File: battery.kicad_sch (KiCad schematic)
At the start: 41 parts, among them J15 Conn_01x02_Pin, J3 Lipo, Q2 AO3401A, Q3 IRLZ44N, Q4 IRLZ44N, Q5 2N7002, SW2 SW_Push, U2 BQ76920PW

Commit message: more lcsc part labels for non generic components
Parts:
- F1: LCSC (none) -> C3762600
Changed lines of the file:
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@@
 			)
 		)
-		(property "LCSC" ""
+		(property "LCSC" "C3762600"
 			(at 105.41 143.51 90)
 			(effects

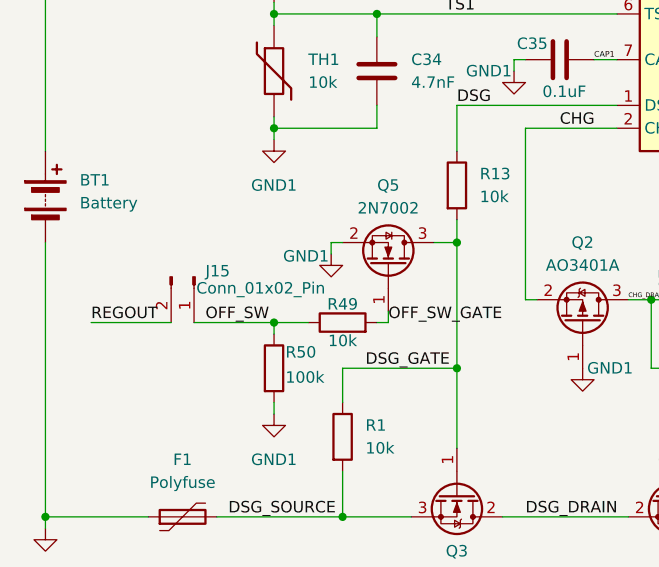
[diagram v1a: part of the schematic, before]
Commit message: Updated edge cuts and drawings from earlier fusion changes and moved traces accordingly
Also fixed jst connectors
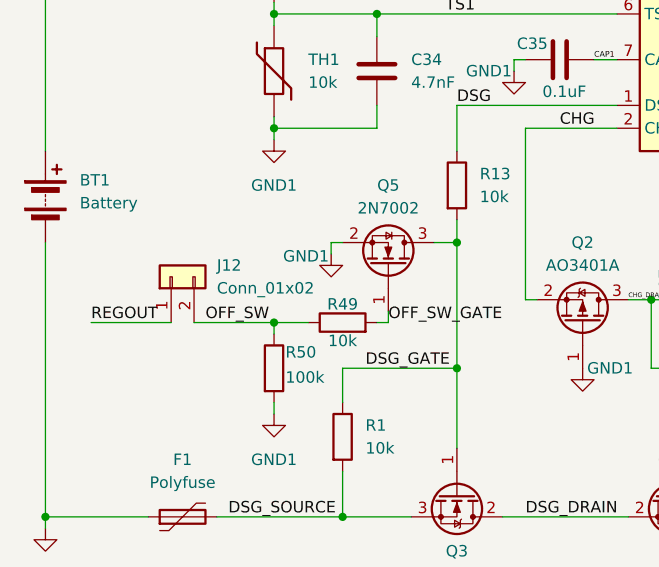
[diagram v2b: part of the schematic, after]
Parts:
- removed J15: Conn_01x02_Pin, Connector:JWT_A3963_1x02_P3.96mm_Vertical, symbol Connector:Conn_01x02_Pin
- added J12: Conn_01x02, Connector_JST:JST_PH_S2B-PH-K_1x02_P2.00mm_Horizontal, symbol Connector_Generic:Conn_01x02
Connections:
- net OFF_SW: now also J12.2 (Pin_2)
- net REGOUT: now also J12.1 (Pin_1)
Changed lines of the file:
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@@
+	)
+	(symbol
+		(lib_id "Connector_Generic:Conn_01x02")
+		(at 104.14 116.84 90)
+		(unit 1)
+		(exclude_from_sim no)
+		(in_bom yes)
+		(on_board yes)
+		(dnp no)
+		(fields_autoplaced yes)
+		(property "Reference" "J12"
+			(at 109.22 115.5699 90)
+			(effects
+				(font
+					(size 1.27 1.27)
+				)
+				(justify right)
+			)
+		)
+		(property "Value" "Conn_01x02"
+			(at 109.22 118.1099 90)
+			(effects
+				(font
+					(size 1.27 1.27)
+				)
+				(justify right)
+			)
+		)
+		(property "Footprint" "Connector_JST:JST_PH_S2B-PH-K_1x02_P2.00mm_Horizontal"
+			(at 104.14 116.84 0)
+			(effects
+				(font
+					(size 1.27 1.27)
+				)
+				(hide yes)
+			)
+		)
+		(property "Datasheet" "~"
+			(at 104.14 116.84 0)
+			(effects
+				(font
+					(size 1.27 1.27)
+				)
+				(hide yes)
+			)
+		)
+		(property "Description" "Generic connector, single row, 01x02, script generated (kicad-library-utils/schlib/autogen/connector/)"
+			(at 104.14 116.84 0)
+			(effects
+				(font
+					(size 1.27 1.27)
+				)
+				(hide yes)
+			)
+		)
+		(pin "1"
+		)
+		(pin "2"
+		)
+		(instances
+			(project ""
+				(path "/2f56b371-1597-47e1-a48d-b7f69d342f77/8e993949-53ac-4d46-9f7d-59c9cf3d33c4"
+					(reference "J12")
+					(unit 1)
+				)
+			)
+		)
 	)
 	(symbol
@@
 					(unit 1)
 				)
-			)
-		)
-	)
-	(symbol
-		(lib_id "Connector:Conn_01x02_Pin")
-		(at 106.68 116.84 270)
-		(unit 1)
-		(exclude_from_sim no)
-		(in_bom yes)
-		(on_board yes)
-		(dnp no)
-		(property "Reference" "J15"
-			(at 107.95 116.2049 90)
-			(effects
-				(font
-					(size 1.27 1.27)
-				)
-				(justify left)
-			)
-		)
-		(property "Value" "Conn_01x02_Pin"
-			(at 106.934 118.11 90)
-			(effects
-				(font
-					(size 1.27 1.27)
-				)
-				(justify left)
-			)
-		)
-		(property "Footprint" "Connector:JWT_A3963_1x02_P3.96mm_Vertical"
-			(at 106.68 116.84 0)
-			(effects
-				(font
-					(size 1.27 1.27)
-				)
-				(hide yes)
-			)
-		)
-		(property "Datasheet" "~"
-			(at 106.68 116.84 0)
-			(effects
-				(font
-					(size 1.27 1.27)
-				)
-				(hide yes)
-			)
-		)
-		(property "Description" "Generic connector, single row, 01x02, script generated"
-			(at 106.68 116.84 0)
-			(effects
-				(font
-					(size 1.27 1.27)
-				)
-				(hide yes)
-			)
-		)
-		(pin "1"
-		)
-		(pin "2"
-		)
-		(instances
-			(project ""
-				(path "/2f56b371-1597-47e1-a48d-b7f69d342f77/8e993949-53ac-4d46-9f7d-59c9cf3d33c4"
-					(reference "J15")
-					(unit 1)
-				)

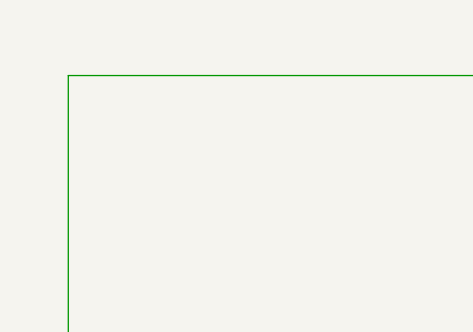
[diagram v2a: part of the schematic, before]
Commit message: started moving traces to be same distance apart to look cleaner
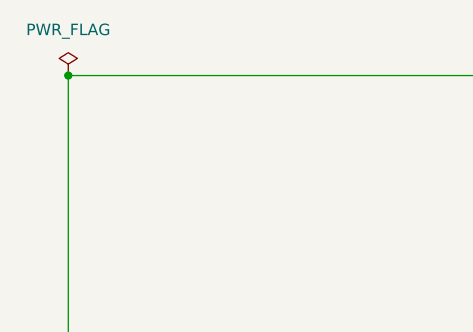
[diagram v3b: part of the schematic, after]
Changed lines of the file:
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@@
+	)
+	(junction
+		(at 90.17 39.37)
+		(diameter 0)
+		(color 0 0 0 0)
 	)
 	(junction
@@
 					(unit 1)
 				)
+			)
+		)
+	)
+	(symbol
+		(lib_id "power:PWR_FLAG")
+		(at 90.17 39.37 0)
+		(unit 1)
+		(exclude_from_sim no)
+		(in_bom yes)
+		(on_board yes)
+		(dnp no)
+		(fields_autoplaced yes)
+		(property "Reference" "#FLG02"
+			(at 90.17 37.465 0)
+			(effects
+				(font
+					(size 1.27 1.27)
+				)
+				(hide yes)
+			)
+		)
+		(property "Value" "PWR_FLAG"
+			(at 90.17 34.29 0)
+			(effects
+				(font
+					(size 1.27 1.27)
+				)
+			)
+		)
+		(property "Footprint" ""
+			(at 90.17 39.37 0)
+			(effects
+				(font
+					(size 1.27 1.27)
+				)
+				(hide yes)
+			)
+		)
+		(property "Datasheet" "~"
+			(at 90.17 39.37 0)
+			(effects
+				(font
+					(size 1.27 1.27)
+				)
+				(hide yes)
+			)
+		)
+		(property "Description" "Special symbol for telling ERC where power comes from"
+			(at 90.17 39.37 0)
+			(effects
+				(font
+					(size 1.27 1.27)
+				)
+				(hide yes)
+			)
+		)
+		(pin "1"
+		)
+		(instances
+			(project ""
+				(path "/2f56b371-1597-47e1-a48d-b7f69d342f77/8e993949-53ac-4d46-9f7d-59c9cf3d33c4"
+					(reference "#FLG02")
+					(unit 1)
+				)

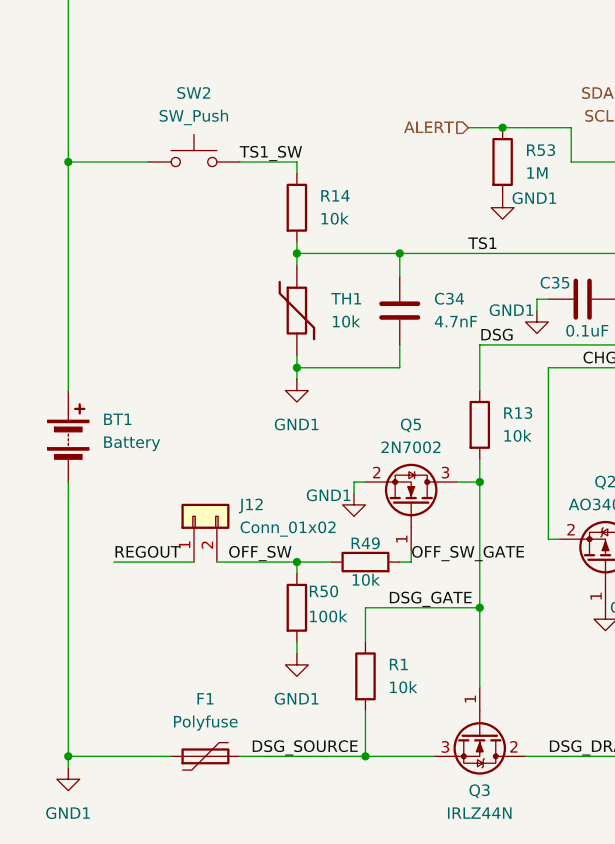
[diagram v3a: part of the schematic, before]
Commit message: moved polyfuse to positive side of battery
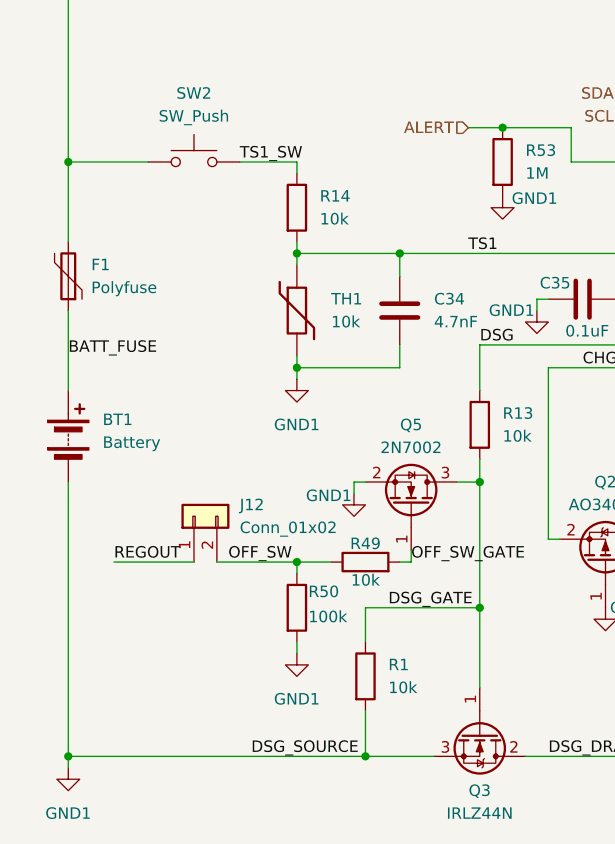
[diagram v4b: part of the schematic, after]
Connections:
- net BATT+: now also F1.2; no longer BT1.1 (+)
- net GND1: now also Q3.3 (S), R1.2; no longer F1.1
- removed net DSG_SOURCE: F1.2, Q3.3 (S), R1.2
- new net BATT_FUSE: BT1.1 (+), F1.1
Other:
- moved on the sheet: F1
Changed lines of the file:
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@@
 	)
 	(junction
-		(at 90.17 77.47)
-		(diameter 0)
-		(color 0 0 0 0)
-	)
-	(junction
 		(at 135.89 127)
 		(diameter 0)
@@
 	)
 	(junction
+		(at 90.17 77.47)
+		(diameter 0)
+		(color 0 0 0 0)
+	)
+	(junction
 		(at 233.68 102.87)
 		(diameter 0)
@@
 	(wire
 		(pts
+			(xy 90.17 93.98) (xy 90.17 102.87)
+		)
+		(stroke
+			(width 0)
+			(type default)
+		)
+	)
+	(wire
+		(pts
 			(xy 233.68 101.6) (xy 233.68 102.87)
 		)
@@
 	(wire
 		(pts
-			(xy 90.17 143.51) (xy 101.6 143.51)
+			(xy 90.17 143.51) (xy 123.19 143.51)
 		)
 		(stroke
@@
 	(wire
 		(pts
+			(xy 90.17 77.47) (xy 90.17 86.36)
+		)
+		(stroke
+			(width 0)
+			(type default)
+		)
+	)
+	(wire
+		(pts
 			(xy 109.22 77.47) (xy 115.57 77.47)
 		)
@@
 	(wire
 		(pts
-			(xy 90.17 77.47) (xy 90.17 102.87)
-		)
-		(stroke
-			(width 0)
-			(type default)
-		)
-	)
-	(wire
-		(pts
 			(xy 171.45 125.73) (xy 171.45 124.46)
 		)
@@
 	(wire
 		(pts
-			(xy 109.22 143.51) (xy 123.19 143.51)
-		)
-		(stroke
-			(width 0)
-			(type default)
-		)
-	)
-	(wire
-		(pts
 			(xy 213.36 50.8) (xy 214.63 50.8)
 		)
@@
 		)
 	)
+	(label "BATT_FUSE"
+		(at 90.17 99.06 0)
+		(effects
+			(font
+				(size 1.27 1.27)
+			)
+			(justify left bottom)
+		)
+	)
 	(label "V3"
 		(at 260.35 85.09 0)
@@
 	(symbol
 		(lib_id "Device:Polyfuse")
-		(at 105.41 143.51 90)
+		(at 90.17 90.17 180)
 		(unit 1)
 		(exclude_from_sim no)
@@
 		(fields_autoplaced yes)
 		(property "Reference" "F1"
-			(at 105.41 137.16 90)
+			(at 92.71 88.8999 0)
 			(effects
 				(font
 					(size 1.27 1.27)
 				)
+				(justify right)
 			)
 		)
 		(property "Value" "Polyfuse"
-			(at 105.41 139.7 90)
+			(at 92.71 91.4399 0)
 			(effects
 				(font
 					(size 1.27 1.27)
 				)
+				(justify right)
 			)
 		)
 		(property "Footprint" "Fuse:Fuse_Bourns_MF-RG900"
-			(at 110.49 142.24 0)
+			(at 88.9 85.09 0)
 			(effects
 				(font
@@
 		)
 		(property "Datasheet" "~"
-			(at 105.41 143.51 0)
+			(at 90.17 90.17 0)
 			(effects
 				(font
@@
 		)
 		(property "Description" "Resettable fuse, polymeric positive temperature coefficient"
-			(at 105.41 143.51 0)
+			(at 90.17 90.17 0)
 			(effects
 				(font
@@
 		)
 		(property "LCSC" "C3762600"
-			(at 105.41 143.51 90)
+			(at 90.17 90.17 90)
 			(effects
 				(font
@@
 		)
 		(property "KLC_S3.3" ""
-			(at 105.41 143.51 90)
+			(at 90.17 90.17 90)
 			(effects
 				(font
@@
 		)
 		(property "KLC_S4.1" ""
-			(at 105.41 143.51 90)
+			(at 90.17 90.17 90)
 			(effects
 				(font
@@
 		)
 		(instances
-			(project ""
+			(project "robot_pcb"
 				(path "/2f56b371-1597-47e1-a48d-b7f69d342f77/8e993949-53ac-4d46-9f7d-59c9cf3d33c4"
 					(reference "F1")
 					(unit 1)
-				)
-			)
-			(project "battery"
-				(path "/5852dc9c-be81-4731-9c95-5e6ebdb17894"
-					(reference "F1")
-					(unit 1)

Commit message: fixed some issues with crystals and other stuff
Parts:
- C1, C2, C3, C4: value 0.1uF -> 1uF
- R10: footprint Resistor_SMD:R_1210_3225Metric -> Resistor_SMD:R_2512_6332Metric; LCSC (none) -> C2903482
- R15: footprint Resistor_SMD:R_0805_2012Metric -> Resistor_SMD:R_1206_3216Metric
- R2, R3, R4, R5: value 470 -> 100; footprint Resistor_SMD:R_0402_1005Metric -> Resistor_SMD:R_0805_2012Metric
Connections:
- net BAT: no longer C37.1, R15.2, U2.9 (REGSRC)
- net BATT+: no longer SW2.1
- net VC1: now also SW2.1
- new net REGSRC: C37.1, R15.2, U2.9 (REGSRC)

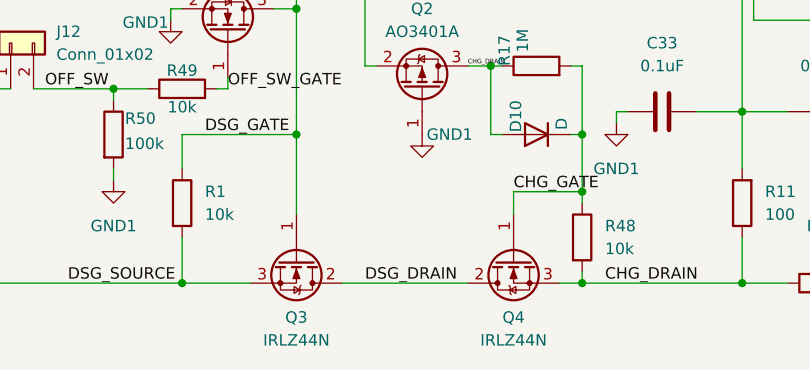
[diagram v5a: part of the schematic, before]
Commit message: replaced tht fets with smd ones in bms
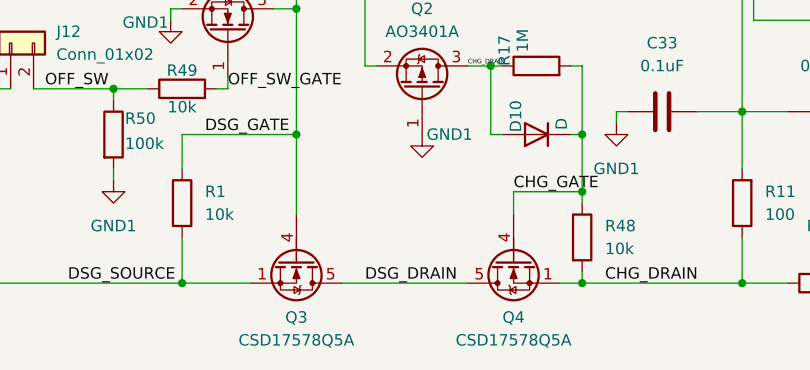
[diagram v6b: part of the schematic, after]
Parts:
- removed Q3, Q4: IRLZ44N, Package_TO_SOT_THT:TO-220-3_Horizontal_TabDown, symbol Transistor_FET:IRLZ44N
- added Q3, Q4: CSD17578Q5A, Package_TO_SOT_SMD:TDSON-8-1, symbol Transistor_FET:CSD17578Q5A
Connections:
- net CHG_DRAIN: now also Q4.1 (S), Q4.2 (S), Q4.3 (S)
- net CHG_GATE: now also Q4.4 (G)
- net DSG_DRAIN: now also Q3.5 (D), Q4.5 (D)
- net DSG_GATE: now also Q3.4 (G)
- net GND1: now also Q3.1 (S), Q3.2 (S), Q3.3 (S)

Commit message: more lcsc parts
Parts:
- R15: LCSC (none) -> C2907369
- R16: LCSC (none) -> C105577
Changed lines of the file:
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@@
 			)
 		)
+		(property "LCSC" "C2907369"
+			(at 166.37 44.45 0)
+			(effects
+				(font
+					(size 1.27 1.27)
+				)
+				(hide yes)
+			)
+		)
 		(pin "1"
 		)
@@
 			)
 		)
-		(property "LCSC" ""
+		(property "LCSC" "C105577"
 			(at 204.47 44.45 0)
 			(effects

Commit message: more lcsc
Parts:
- BT1: LCSC (none) -> C98733
- C1, C2, C3, C4: LCSC (none) -> C29266
- C32, C33, C35, C5: value 0.1uF -> 100nF
- C38: LCSC C52923 -> C368809
- R1, R13, R14, R48, R49: LCSC (none) -> C60490
- R11, R12: LCSC (none) -> C105588
- R17, R53: LCSC (none) -> C138033
- R2, R3, R4, R5: LCSC (none) -> C105577
- R50: LCSC (none) -> C60491
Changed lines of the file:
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@@
 			)
 		)
-		(property "LCSC" ""
+		(property "LCSC" "C60490"
 			(at 115.57 82.55 0)
 			(effects
@@
 			)
 		)
-		(property "LCSC" ""
+		(property "LCSC" "C105588"
 			(at 203.2 134.62 0)
 			(effects
@@
 			)
 		)
-		(property "Value" "0.1uF"
+		(property "Value" "100nF"
 			(at 194.31 119.38 90)
 			(effects
@@
 			)
 		)
-		(property "LCSC" ""
+		(property "LCSC" "C105577"
 			(at 247.65 133.35 90)
 			(effects
@@
 			)
 		)
+		(property "LCSC" "C60490"
+			(at 167.64 138.43 0)
+			(effects
+				(font
+					(size 1.27 1.27)
+				)
+				(hide yes)
+			)
+		)
 		(pin "2"
 		)
@@
 			)
 		)
-		(property "LCSC" ""
+		(property "LCSC" "C29266"
 			(at 233.68 107.95 0)
 			(effects
@@
 			)
 		)
-		(property "LCSC" ""
+		(property "LCSC" "C98733"
 			(at 90.17 107.95 0)
 			(effects
@@
 			)
 		)
-		(property "Value" "0.1uF"
+		(property "Value" "100nF"
 			(at 176.53 119.38 90)
 			(effects
@@
 			)
 		)
-		(property "LCSC" ""
+		(property "LCSC" "C60490"
 			(at 123.19 134.62 0)
 			(effects
@@
 			)
 		)
-		(property "LCSC" ""
+		(property "LCSC" "C105588"
 			(at 185.42 134.62 0)
 			(effects
@@
 			)
 		)
-		(property "LCSC" ""
+		(property "LCSC" "C29266"
 			(at 233.68 97.79 0)
 			(effects
@@
 			)
 		)
-		(property "LCSC" ""
+		(property "LCSC" "C29266"
 			(at 233.68 128.27 0)
 			(effects
@@
 			)
 		)
+		(property "LCSC" ""
+			(at 160.02 140.97 90)
+			(effects
+				(font
+					(size 1.27 1.27)
+				)
+				(hide yes)
+			)
+		)
 		(pin "3"
 		)
@@
 			)
 		)
+		(property "LCSC" "C60491"
+			(at 115.57 127 0)
+			(effects
+				(font
+					(size 1.27 1.27)
+				)
+				(hide yes)
+			)
+		)
 		(pin "2"
 		)
@@
 			)
 		)
-		(property "LCSC" ""
+		(property "LCSC" "C138033"
 			(at 162.56 119.38 0)
 			(effects
@@
 			)
 		)
-		(property "LCSC" ""
+		(property "LCSC" "C105577"
 			(at 247.65 92.71 90)
 			(effects
@@
 			)
 		)
-		(property "LCSC" ""
+		(property "LCSC" "C105577"
 			(at 247.65 113.03 90)
 			(effects
@@
 			)
 		)
+		(property "LCSC" "C138033"
+			(at 138.43 77.47 0)
+			(effects
+				(font
+					(size 1.27 1.27)
+				)
+				(hide yes)
+			)
+		)
 		(pin "1"
 		)
@@
 			)
 		)
-		(property "Value" "0.1uF"
+		(property "Value" "100nF"
 			(at 212.09 119.38 90)
 			(effects
@@
 			)
 		)
-		(property "LCSC" ""
+		(property "LCSC" "C29266"
 			(at 233.68 118.11 0)
 			(effects
@@
 			)
 		)
-		(property "Value" "0.1uF"
+		(property "Value" "100nF"
 			(at 147.828 96.266 90)
 			(effects
@@
 			)
 		)
-		(property "LCSC" "C52923"
+		(property "LCSC" "C368809"
 			(at 209.55 50.8 90)
 			(effects
@@
 			)
 		)
+		(property "LCSC" ""
+			(at 135.89 140.97 90)
+			(effects
+				(font
+					(size 1.27 1.27)
+				)
+				(hide yes)
+			)
+		)
 		(pin "3"
 		)
@@
 			)
 		)
+		(property "LCSC" "C60490"
+			(at 123.19 121.92 90)
+			(effects
+				(font
+					(size 1.27 1.27)
+				)
+				(hide yes)
+			)
+		)
 		(pin "1"
 		)
@@
 			)
 		)
-		(property "LCSC" ""
+		(property "LCSC" "C105577"
 			(at 247.65 102.87 90)
 			(effects
@@
 			)
 		)
-		(property "LCSC" ""
+		(property "LCSC" "C60490"
 			(at 135.89 106.68 0)
 			(effects
